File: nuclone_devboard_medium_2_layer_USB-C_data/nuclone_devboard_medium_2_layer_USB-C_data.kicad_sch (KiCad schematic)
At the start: 38 parts, among them J1 JTAG_2X05, J2 TYPE-C-31-M-12, J3 nuclone_medium_left, J4 nuclone_medium_right, SW1 RESET, SW2 Bootloader, U1 MCP1702-3.3V, U2 TPESD0504C6

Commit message: small updates
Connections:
- net Bootloader renamed BOOT
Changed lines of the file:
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@@
     (effects (font (size 1.27 1.27)) (justify left bottom))
   )
-  (label "Bootloader" (at 241.3 158.75 0) (fields_autoplaced)
+  (label "BOOT" (at 241.3 158.75 0) (fields_autoplaced)
     (effects (font (size 1.27 1.27)) (justify left bottom))
   )
@@
     (effects (font (size 1.27 1.27)) (justify right bottom))
   )
-  (label "Bootloader" (at 96.52 143.51 0) (fields_autoplaced)
+  (label "BOOT" (at 96.52 143.51 0) (fields_autoplaced)
     (effects (font (size 1.27 1.27)) (justify left bottom))
   )
@@
     )
     (instances
-      (project "nuclone_devboard_medium"
+      (project "nuclone_devboard_medium_2_layer_USB-C_data"
         (path "/f714ce77-1b03-46de-8ce2-42d10401024e"
           (reference "N1") (unit 1)
@@
     (pin "9")
     (instances
-      (project "nuclone_devboard_medium"
+      (project "nuclone_devboard_medium_2_layer_USB-C_data"
         (path "/f714ce77-1b03-46de-8ce2-42d10401024e"
           (reference "J1") (unit 1)
@@
     (pin "2")
     (instances
-      (project "nuclone_devboard_medium"
+      (project "nuclone_devboard_medium_2_layer_USB-C_data"
         (path "/f714ce77-1b03-46de-8ce2-42d10401024e"
           (reference "FB1") (unit 1)
@@
     (pin "2")
     (instances
-      (project "nuclone_devboard_medium"
+      (project "nuclone_devboard_medium_2_layer_USB-C_data"
         (path "/f714ce77-1b03-46de-8ce2-42d10401024e"
           (reference "F1") (unit 1)
@@
     (pin "2")
     (instances
-      (project "nuclone_devboard_medium"
+      (project "nuclone_devboard_medium_2_layer_USB-C_data"
         (path "/f714ce77-1b03-46de-8ce2-42d10401024e"
           (reference "C2") (unit 1)
@@
     (pin "1")
     (instances
-      (project "nuclone_devboard_medium"
+      (project "nuclone_devboard_medium_2_layer_USB-C_data"
         (path "/f714ce77-1b03-46de-8ce2-42d10401024e"
           (reference "#FLG01") (unit 1)
@@
     )
     (instances
-      (project "nuclone_devboard_medium"
+      (project "nuclone_devboard_medium_2_layer_USB-C_data"
         (path "/f714ce77-1b03-46de-8ce2-42d10401024e"
           (reference "H4") (unit 1)
@@
     )
     (instances
-      (project "nuclone_devboard_medium"
+      (project "nuclone_devboard_medium_2_layer_USB-C_data"
         (path "/f714ce77-1b03-46de-8ce2-42d10401024e"
           (reference "H3") (unit 1)
@@
     )
     (instances
-      (project "nuclone_devboard_medium"
+      (project "nuclone_devboard_medium_2_layer_USB-C_data"
         (path "/f714ce77-1b03-46de-8ce2-42d10401024e"
           (reference "H2") (unit 1)
@@
     )
     (instances
-      (project "nuclone_devboard_medium"
+      (project "nuclone_devboard_medium_2_layer_USB-C_data"
         (path "/f714ce77-1b03-46de-8ce2-42d10401024e"
           (reference "H1") (unit 1)
@@
     )
     (instances
-      (project "nuclone_devboard_medium"
+      (project "nuclone_devboard_medium_2_layer_USB-C_data"
         (path "/f714ce77-1b03-46de-8ce2-42d10401024e"
           (reference "N2") (unit 1)
@@
     (pin "3")
     (instances
-      (project "nuclone_devboard_medium"
+      (project "nuclone_devboard_medium_2_layer_USB-C_data"
         (path "/f714ce77-1b03-46de-8ce2-42d10401024e"
           (reference "U1") (unit 1)
@@
     (pin "2")
     (instances
-      (project "nuclone_devboard_medium"
+      (project "nuclone_devboard_medium_2_layer_USB-C_data"
         (path "/f714ce77-1b03-46de-8ce2-42d10401024e"
           (reference "C1") (unit 1)
@@
     (pin "9")
     (instances
-      (project "nuclone_devboard_medium"
+      (project "nuclone_devboard_medium_2_layer_USB-C_data"
         (path "/f714ce77-1b03-46de-8ce2-42d10401024e"
           (reference "J3") (unit 1)
@@
     (pin "9")
     (instances
-      (project "nuclone_devboard_medium"
+      (project "nuclone_devboard_medium_2_layer_USB-C_data"
         (path "/f714ce77-1b03-46de-8ce2-42d10401024e"
           (reference "J4") (unit 1)
@@
     )
     (instances
-      (project "nuclone_devboard_medium"
+      (project "nuclone_devboard_medium_2_layer_USB-C_data"
         (path "/f714ce77-1b03-46de-8ce2-42d10401024e"
           (reference "N3") (unit 1)
@@
     (pin "2")
     (instances
-      (project "nuclone_devboard_medium"
+      (project "nuclone_devboard_medium_2_layer_USB-C_data"
         (path "/f714ce77-1b03-46de-8ce2-42d10401024e"
           (reference "SW1") (unit 1)
@@
     (pin "S")
     (instances
-      (project "nuclone_devboard_medium"
+      (project "nuclone_devboard_medium_2_layer_USB-C_data"
         (path "/f714ce77-1b03-46de-8ce2-42d10401024e"
           (reference "J2") (unit 1)
@@
     (pin "2")
     (instances
-      (project "nuclone_devboard_medium"
+      (project "nuclone_devboard_medium_2_layer_USB-C_data"
         (path "/f714ce77-1b03-46de-8ce2-42d10401024e"
           (reference "R1") (unit 1)
@@
     (pin "2")
     (instances
-      (project "nuclone_devboard_medium"
+      (project "nuclone_devboard_medium_2_layer_USB-C_data"
         (path "/f714ce77-1b03-46de-8ce2-42d10401024e"
           (reference "R2") (unit 1)
@@
     (pin "2")
     (instances
-      (project "nuclone_devboard_medium"
+      (project "nuclone_devboard_medium_2_layer_USB-C_data"
         (path "/f714ce77-1b03-46de-8ce2-42d10401024e"
           (reference "R3") (unit 1)
@@
     (pin "2")
     (instances
-      (project "nuclone_devboard_medium"
+      (project "nuclone_devboard_medium_2_layer_USB-C_data"
         (path "/f714ce77-1b03-46de-8ce2-42d10401024e"
           (reference "R4") (unit 1)
@@
     (pin "2")
     (instances
-      (project "nuclone_devboard_medium"
+      (project "nuclone_devboard_medium_2_layer_USB-C_data"
         (path "/f714ce77-1b03-46de-8ce2-42d10401024e"
           (reference "R5") (unit 1)
@@
     (pin "2")
     (instances
-      (project "nuclone_devboard_medium"
+      (project "nuclone_devboard_medium_2_layer_USB-C_data"
         (path "/f714ce77-1b03-46de-8ce2-42d10401024e"
           (reference "R6") (unit 1)
@@
     )
     (instances
-      (project "nuclone_devboard_medium"
+      (project "nuclone_devboard_medium_2_layer_USB-C_data"
         (path "/f714ce77-1b03-46de-8ce2-42d10401024e"
           (reference "N4") (unit 1)
@@
     (pin "2")
     (instances
-      (project "nuclone_devboard_medium"
+      (project "nuclone_devboard_medium_2_layer_USB-C_data"
         (path "/f714ce77-1b03-46de-8ce2-42d10401024e"
           (reference "R13") (unit 1)
@@
     (pin "1")
     (instances
-      (project "nuclone_devboard_medium"
+      (project "nuclone_devboard_medium_2_layer_USB-C_data"
         (path "/f714ce77-1b03-46de-8ce2-42d10401024e"
           (reference "C14") (unit 1)
@@
     (pin "2")
     (instances
-      (project "nuclone_devboard_medium"
+      (project "nuclone_devboard_medium_2_layer_USB-C_data"
         (path "/f714ce77-1b03-46de-8ce2-42d10401024e"
           (reference "R14") (unit 1)
@@
     (pin "2")
     (instances
-      (project "nuclone_devboard_medium"
+      (project "nuclone_devboard_medium_2_layer_USB-C_data"
         (path "/f714ce77-1b03-46de-8ce2-42d10401024e"
           (reference "D2") (unit 1)
@@
     (pin "2")
     (instances
-      (project "nuclone_devboard_medium"
+      (project "nuclone_devboard_medium_2_layer_USB-C_data"
         (path "/f714ce77-1b03-46de-8ce2-42d10401024e"
           (reference "R7") (unit 1)
@@
     (pin "2")
     (instances
-      (project "nuclone_devboard_medium"
+      (project "nuclone_devboard_medium_2_layer_USB-C_data"
         (path "/f714ce77-1b03-46de-8ce2-42d10401024e"
           (reference "C17") (unit 1)
@@
     (pin "2")
     (instances
-      (project "nuclone_devboard_medium"
+      (project "nuclone_devboard_medium_2_layer_USB-C_data"
         (path "/f714ce77-1b03-46de-8ce2-42d10401024e"
           (reference "SW2") (unit 1)
@@
     (pin "2")
     (instances
-      (project "nuclone_devboard_medium"
+      (project "nuclone_devboard_medium_2_layer_USB-C_data"
         (path "/f714ce77-1b03-46de-8ce2-42d10401024e"
           (reference "R8") (unit 1)
@@
     )
     (instances
-      (project "nuclone_devboard_medium"
+      (project "nuclone_devboard_medium_2_layer_USB-C_data"
         (path "/f714ce77-1b03-46de-8ce2-42d10401024e"
           (reference "N5") (unit 1)
@@
     (pin "2")
     (instances
-      (project "nuclone_devboard_medium"
+      (project "nuclone_devboard_medium_2_layer_USB-C_data"
         (path "/f714ce77-1b03-46de-8ce2-42d10401024e"
           (reference "C6") (unit 1)
@@
     (pin "2")
     (instances
-      (project "nuclone_devboard_medium"
+      (project "nuclone_devboard_medium_2_layer_USB-C_data"
         (path "/f714ce77-1b03-46de-8ce2-42d10401024e"
           (reference "R9") (unit 1)
@@
         )
       )
-      (project "nuclone_devboard_medium"
+      (project "nuclone_devboard_medium_2_layer_USB-C_data"
         (path "/f714ce77-1b03-46de-8ce2-42d10401024e"
           (reference "U2") (unit 1)
@@
         )
       )
-      (project "nuclone_devboard_medium"
+      (project "nuclone_devboard_medium_2_layer_USB-C_data"
         (path "/f714ce77-1b03-46de-8ce2-42d10401024e"
           (reference "C4") (unit 1)
@@
     (pin "1")
     (instances
-      (project "nuclone_devboard_medium"
+      (project "nuclone_devboard_medium_2_layer_USB-C_data"
         (path "/f714ce77-1b03-46de-8ce2-42d10401024e"
           (reference "C5") (unit 1)
@@
     )
     (instances
-      (project "nuclone_devboard_medium"
+      (project "nuclone_devboard_medium_2_layer_USB-C_data"
         (path "/f714ce77-1b03-46de-8ce2-42d10401024e" (page "2"))
       )

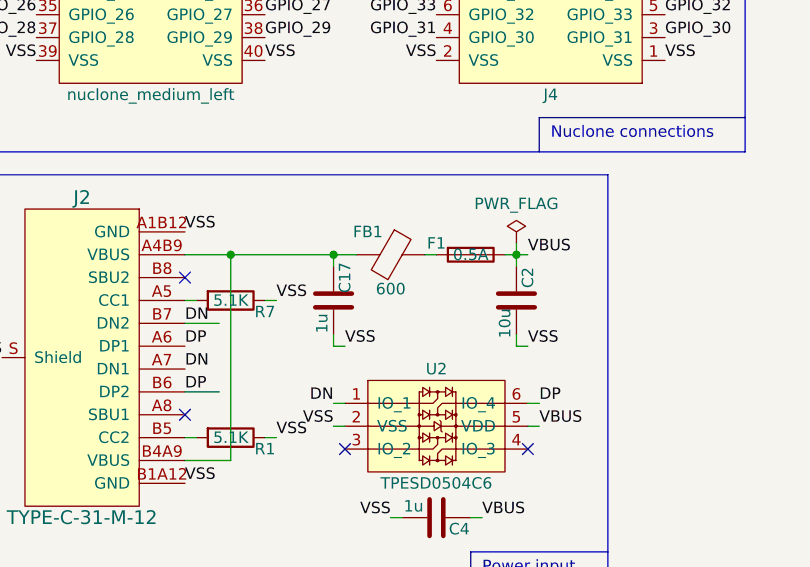
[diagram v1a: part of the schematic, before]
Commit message: added diode, updated library
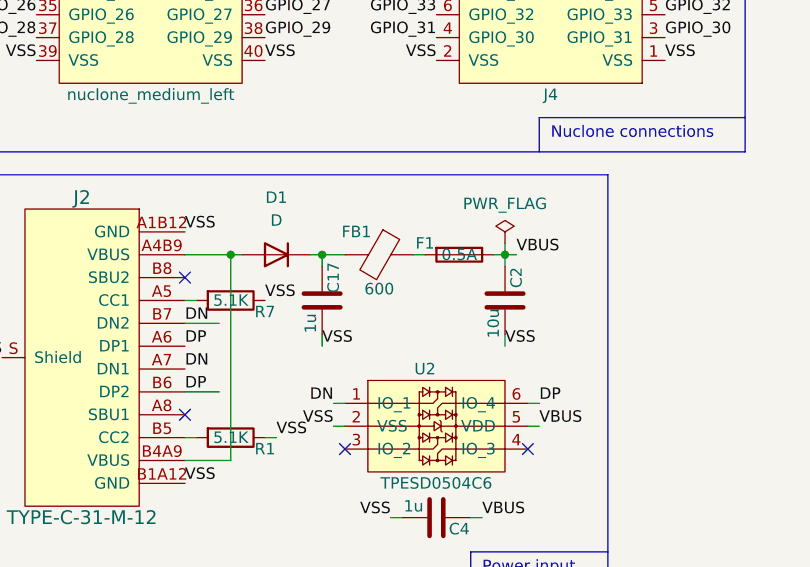
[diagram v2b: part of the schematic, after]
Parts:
- added D1: D, symbol Device:D
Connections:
- net at C17.2, FB1.2: now also D1.1 (K); no longer J2.A4B9 (VBUS), J2.B4A9 (VBUS)
- new net: D1.2 (A), J2.A4B9 (VBUS), J2.B4A9 (VBUS)
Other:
- moved on the sheet: C17, C2, F1, FB1

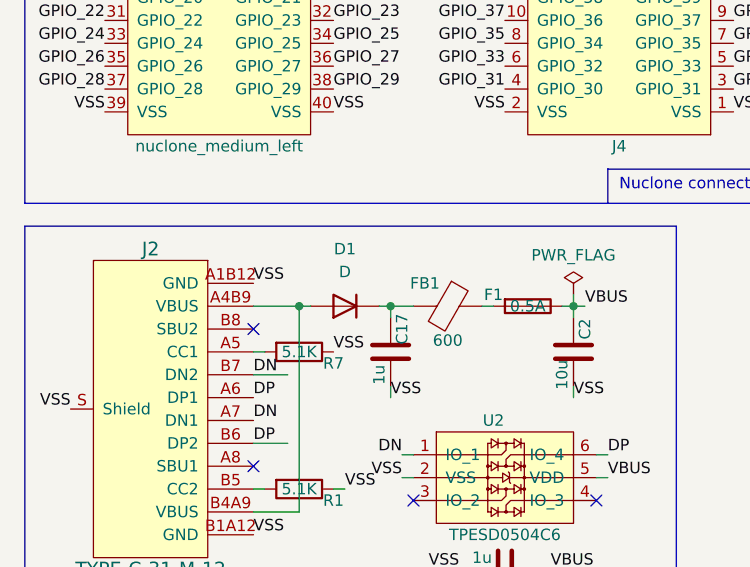
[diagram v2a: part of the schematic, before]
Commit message: added diode in series
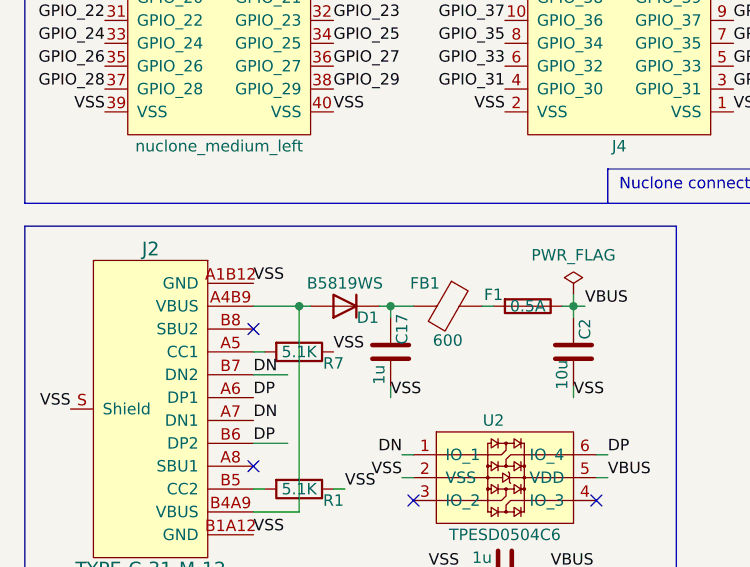
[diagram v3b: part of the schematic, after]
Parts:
- D1: value D -> B5819WS; footprint (none) -> SquantorDiodes:SOD-323-nexperia-hand
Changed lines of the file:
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@@
   )
   (symbol (lib_id "Device:D") (at 50.8 90.17 180) (unit 1)
-    (in_bom yes) (on_board yes) (dnp no) (fields_autoplaced)
-    (property "Reference" "D1" (at 50.8 83.82 0)
+    (in_bom yes) (on_board yes) (dnp no)
+    (property "Reference" "D1" (at 53.34 91.44 0)
       (effects (font (size 1.27 1.27)))
     )
-    (property "Value" "D" (at 50.8 86.36 0)
+    (property "Value" "B5819WS" (at 50.8 87.63 0)
       (effects (font (size 1.27 1.27)))
     )
-    (property "Footprint" "" (at 50.8 90.17 0)
+    (property "Footprint" "SquantorDiodes:SOD-323-nexperia-hand" (at 50.8 90.17 0)
       (effects (font (size 1.27 1.27)) hide)
     )

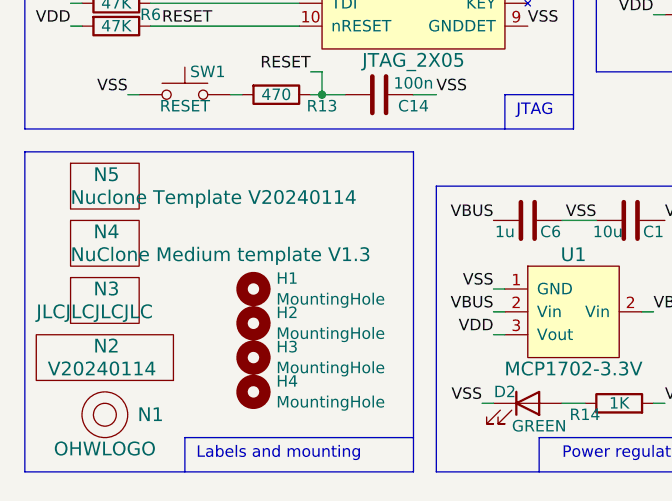
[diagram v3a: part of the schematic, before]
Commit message: updated versionnumbers, aligned mounting holes
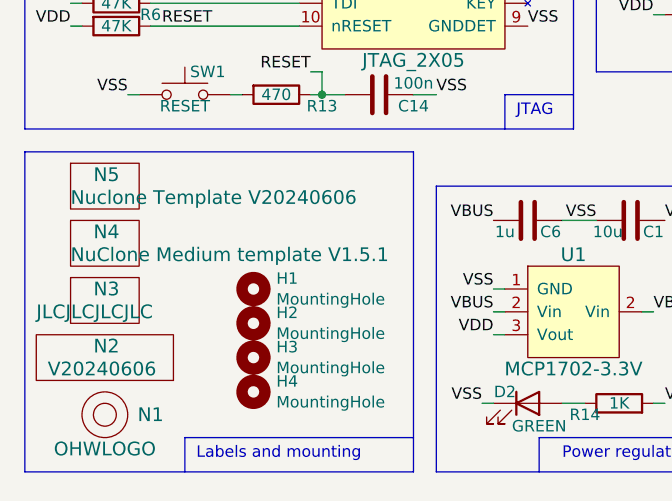
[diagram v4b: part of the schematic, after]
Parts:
- N2: value V20240114 -> V20240606
- N4: value NuClone Medium template V1.3 -> NuClone Medium template V1.5.1
- N5: value Nuclone Template V20240114 -> Nuclone Template V20240606
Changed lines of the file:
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@@
       (effects (font (size 1.524 1.524)) (justify left))
     )
-    (property "Value" "V20240114" (at 17.78 182.88 0)
+    (property "Value" "V20240606" (at 17.78 182.88 0)
       (effects (font (size 1.524 1.524)) (justify left))
     )
@@
       (effects (font (size 1.524 1.524)) (justify left))
     )
-    (property "Value" "NuClone Medium template V1.3" (at 20.32 170.18 0)
+    (property "Value" "NuClone Medium template V1.5.1" (at 20.32 170.18 0)
       (effects (font (size 1.524 1.524)) (justify left))
     )
@@
       (effects (font (size 1.524 1.524)) (justify left))
     )
-    (property "Value" "Nuclone Template V20240114" (at 20.32 163.83 0)
-      (effects (font (size 1.524 1.524)) (justify left))
-    )
+    (property "Value" "Nuclone Template V20240606" (at 20.32 163.83 0)
+      (effects (font (size 1.524 1.524)) (justify left))
+    )
